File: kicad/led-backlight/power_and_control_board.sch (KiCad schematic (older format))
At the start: 5 parts, among them SW1 SW_MEC_5E, U3 AMS1117-3.3

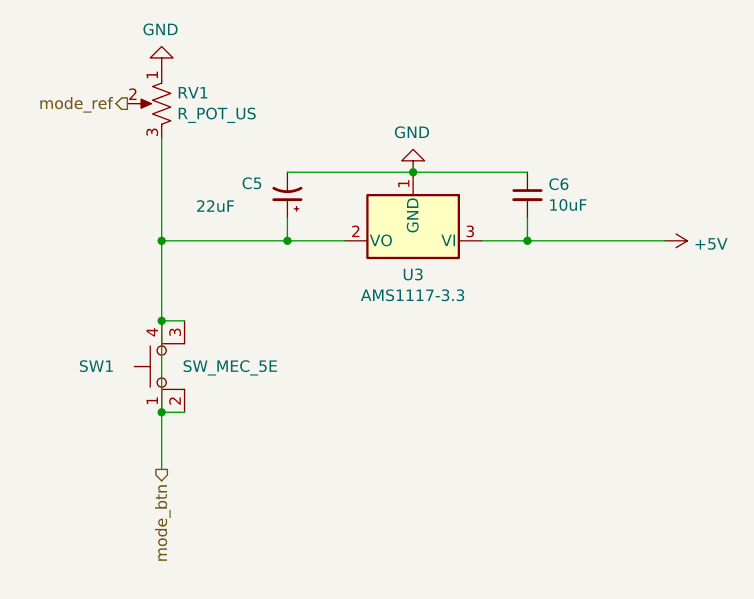
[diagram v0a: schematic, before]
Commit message: add board stackup
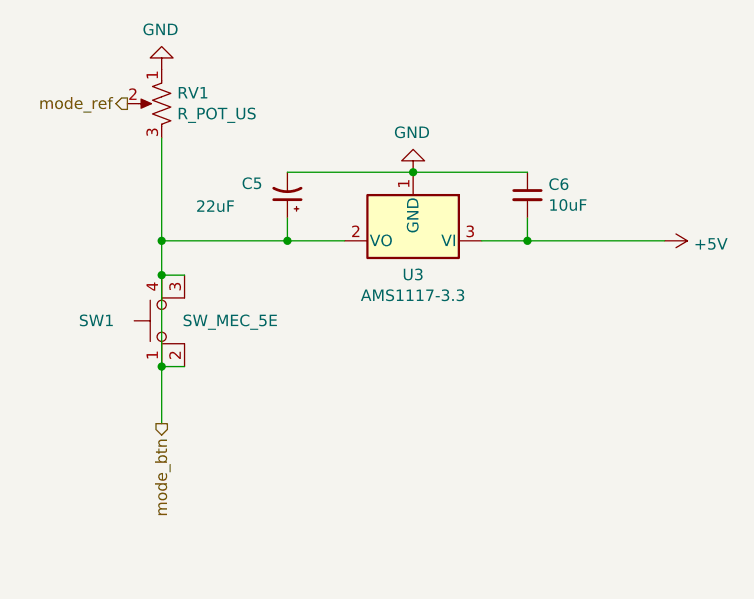
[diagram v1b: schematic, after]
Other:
- moved on the sheet: SW1
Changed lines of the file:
@@
 L Switch:SW_MEC_5E SW1
 U 1 1 60E66D50
-P 5450 4100
-F 0 "SW1" V 5450 4485 50  0000 C CNN
-F 1 "SW_MEC_5E" V 5450 3900 50  0000 C CNN
-F 2 "Button_Switch_THT:SW_PUSH-12mm" H 5450 4400 50  0001 C CNN
-F 3 "http://www.apem.com/int/index.php?controller=attachment&id_attachment=1371" H 5450 4400 50  0001 C CNN
-F 4 "0" H 5450 4100 50  0001 C CNN "JLCPCB BOM"
-	1    5450 4100
+P 5450 3900
+F 0 "SW1" V 5450 4285 50  0000 C CNN
+F 1 "SW_MEC_5E" V 5450 3700 50  0000 C CNN
+F 2 "Button_Switch_THT:SW_PUSH-12mm" H 5450 4200 50  0001 C CNN
+F 3 "http://www.apem.com/int/index.php?controller=attachment&id_attachment=1371" H 5450 4200 50  0001 C CNN
+F 4 "0" H 5450 3900 50  0001 C CNN "JLCPCB BOM"
+	1    5450 3900
 	0    -1   -1   0
 $EndComp
 Text HLabel 5200 2950 0    50   Output ~ 0
 mode_ref
-Text HLabel 5350 4550 3    50   Output ~ 0
+Text HLabel 5350 4350 3    50   Output ~ 0
 mode_btn
 Wire Wire Line
@@
 Connection ~ 5900 3550
 Wire Wire Line
-	5350 3900 5450 3900
+	5350 3700 5450 3700
+Connection ~ 5350 3700
 Wire Wire Line
-	5350 3550 5350 3900
-Connection ~ 5350 3550
-Connection ~ 5350 3900
+	5350 3700 5350 4100
 Wire Wire Line
-	5350 3900 5350 4300
+	5350 4100 5450 4100
+Connection ~ 5350 4100
 Wire Wire Line
-	5350 4300 5450 4300
-Connection ~ 5350 4300
-Wire Wire Line
-	5350 4300 5350 4550
+	5350 4100 5350 4350
 $Comp
 L power:GND #PWR06
@@
 	-1   0    0    1
 $EndComp
-Wire Wire Line
-	6950 3550 7550 3550
 $Comp
 L Device:C_Small C6
@@
 	1    0    0    -1
 $EndComp
+Wire Wire Line
+	6950 3550 7550 3550
+Wire Wire Line
+	5350 3700 5350 3550
+Connection ~ 5350 3550
 $EndSCHEMATC
